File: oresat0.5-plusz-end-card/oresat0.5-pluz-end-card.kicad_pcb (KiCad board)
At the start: 4 copper layers, 99.8 x 94.6 mm, 30 parts, among them J1 J-SAMTEC-TFM-120-01-L-D-RA, J2 Harwin M55-7101242R, J3 Harwin M55-7101242R, J4 Harwin M55-7101242R, J5 Harwin M55-7101242R, J6 Conn_Coaxial

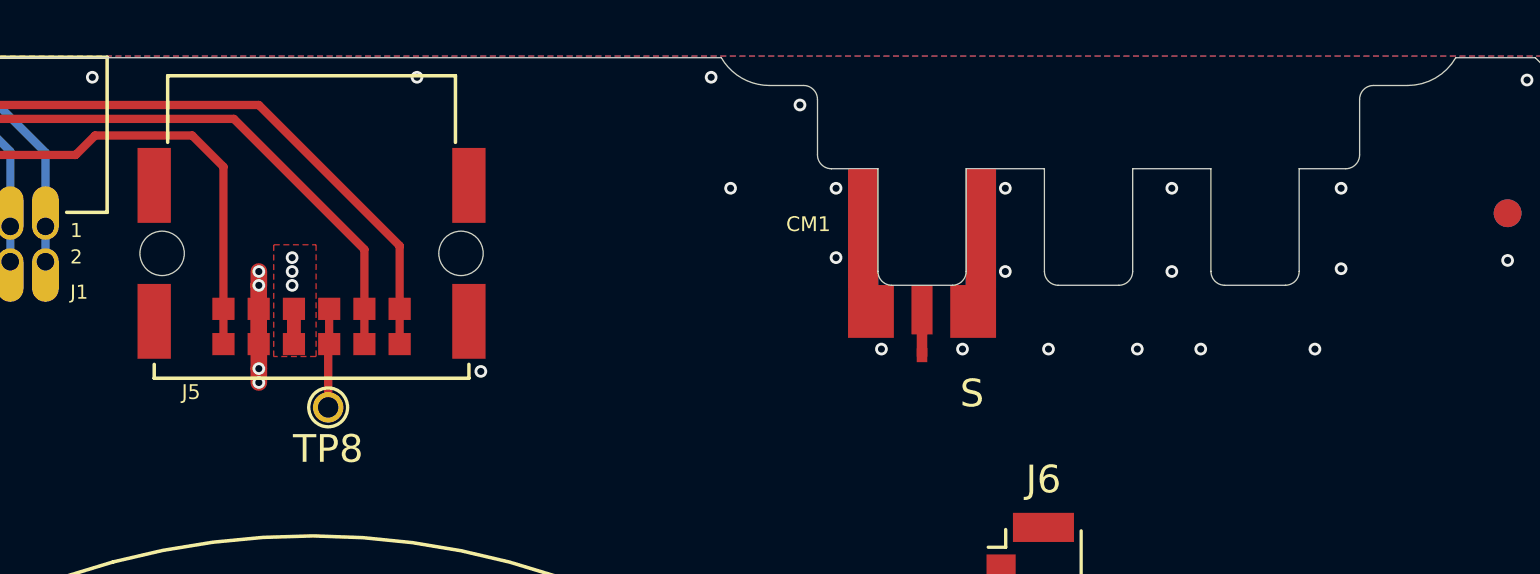
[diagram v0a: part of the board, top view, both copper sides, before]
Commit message: Updated +Z end card connector symbols
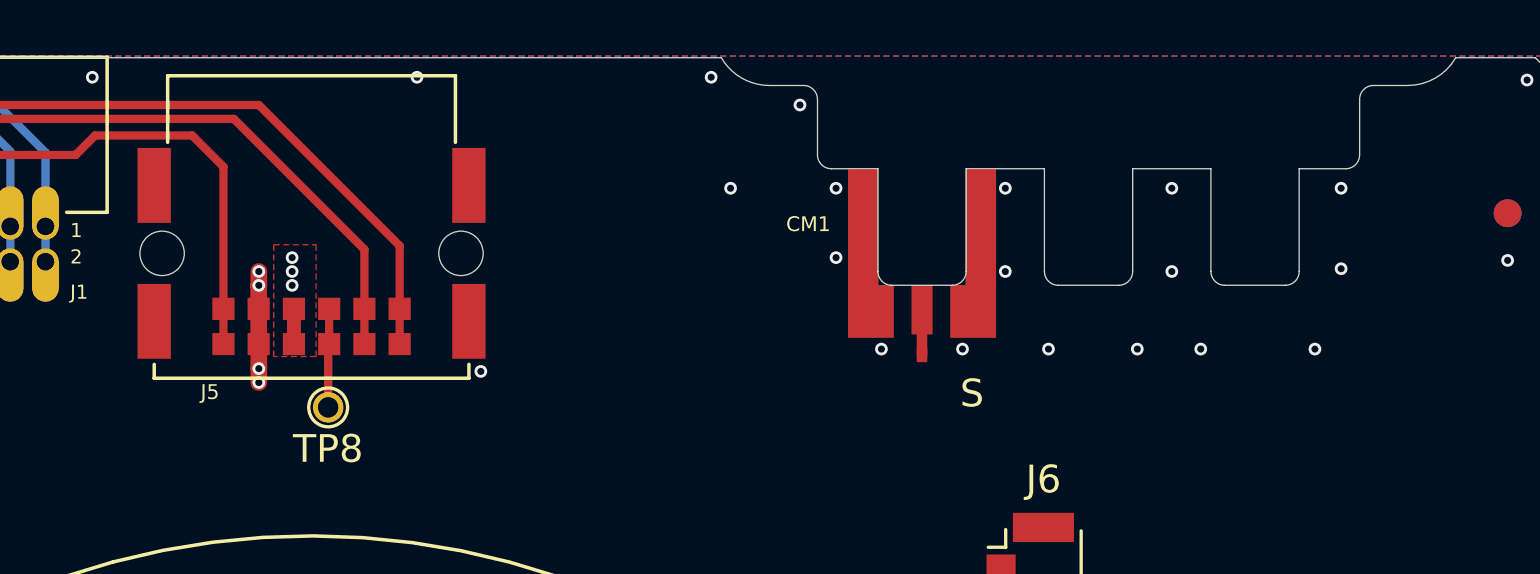
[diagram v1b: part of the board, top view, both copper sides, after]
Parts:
- CF1: footprint plusz-end-card-with-turnstile:HARWIN-M55-60X1242R -> oresat-connectors:J-Harwin-M55-60X1242R
- J2, J3, J4, J5: footprint oresat-footprints:J-Harwin-M55-7101242R -> oresat-connectors:J-Harwin-M55-7101242R
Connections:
- net Net-(J2-Pad7) renamed /-X_AUX
- net Net-(J3-Pad7) renamed /+Y_AUX
- net Net-(J4-Pad7) renamed /+X_AUX
- net Net-(J5-Pad7) renamed /-Y_AUX
